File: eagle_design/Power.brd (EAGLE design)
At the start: 55.9 x 63.2 mm, 17 parts, among them K1 G5LE, K2 G5LE, K3 G5LE

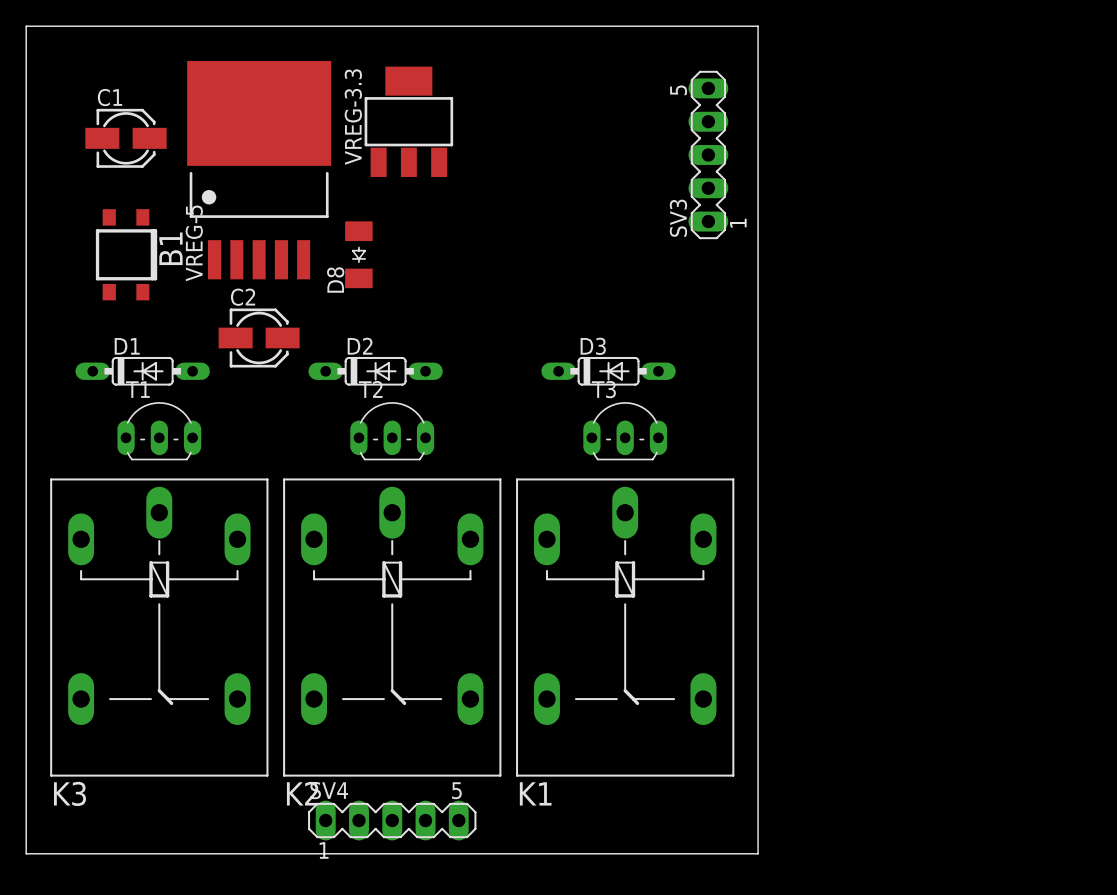
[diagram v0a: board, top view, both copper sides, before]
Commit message: split into three boards and choose new mcu
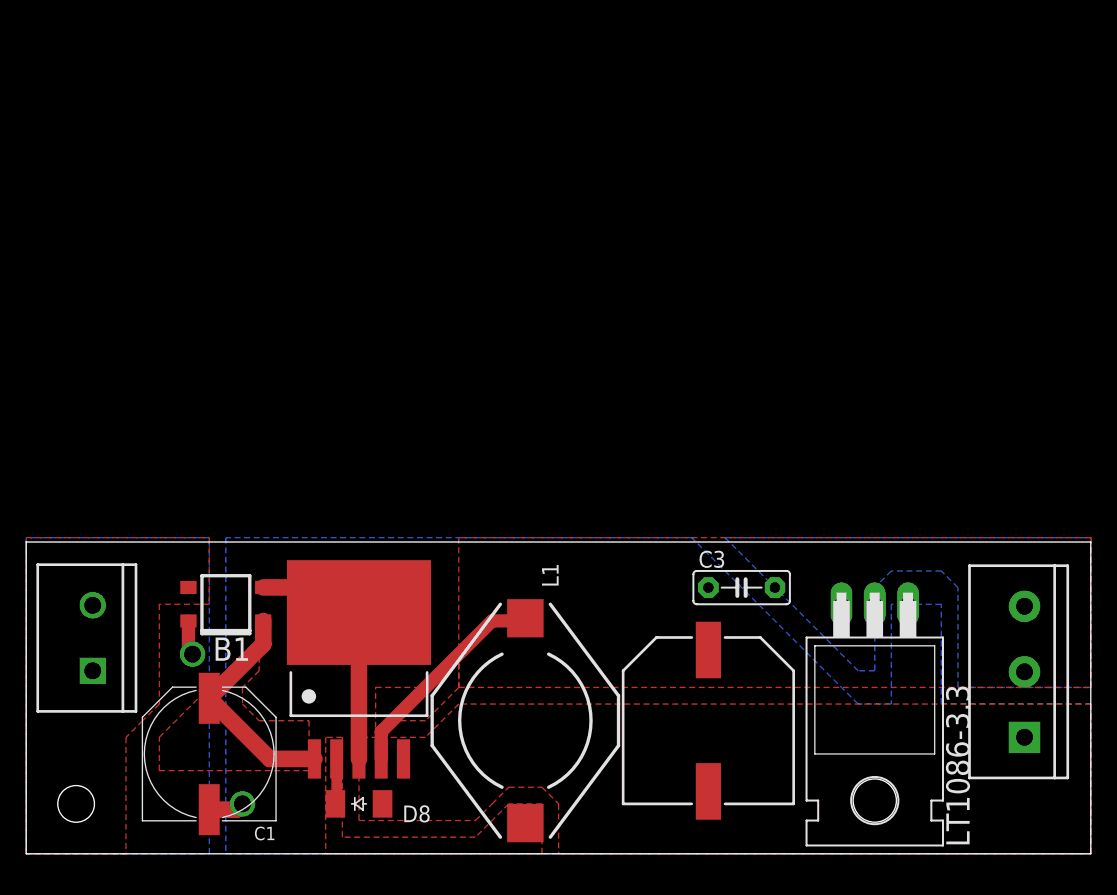
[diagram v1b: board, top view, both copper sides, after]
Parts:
- removed D1, D2, D3: 1N4148DO35-7, diode:DO35-7
- removed K1, K2, K3: G5LE, relay:G5LE
- removed SV3, SV4: (no value), con-lstb:MA05-1
- removed T1, T2, T3: (no value), transistor-neu-to92:TO92-EBC
- removed VREG-3.3: (no value), linear-technology:SOT223
- added C3: 10uF, capacitor-wima:C5B2.5
- added L1: 330uH, TylersLib:DO3316P
- added LT1086-3.3: 317T, linear:TO220H
- added U$1: SCREWTERMINAL-3, SparkFun-Connectors:SCREWTERMINAL-5MM-3
- added U$2: SCREWTERMINAL-2, SparkFun-Connectors:SCREWTERMINAL-5MM-2
- C1: device rcl:153CLV-0405 -> rcl:PANASONIC_G
- C2: value 330uF -> 300uF; device rcl:153CLV-0405 -> rc-master:CSV-H
- moved C1 47.4 mm to (14.0, 7.62), turned to 90 degrees
- moved C2 45.0 mm to (52.1, 10.2), turned to 270 degrees
- moved D8 41.9 mm to (25.4, 3.81), turned to 0 degrees
- moved VREG-5 38.9 mm to (20.3, 5.08)
- moved B1 27.7 mm to (15.2, 19.1), turned to 90 degrees
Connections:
- net N$1 renamed VUNREG
- removed net 3.3+: SV3.5, VREG-3.3.3
- removed net 5V+: C2.+, D1.C, D2.C, D3.C, K1.1, K2.1, K3.1, VREG-3.3.1, VREG-5.4
- removed net AC: SV3.2, T2.B
- removed net FAN: SV3.1, T1.B
- removed net G: K3.S, SV4.1
- removed net HEAT: SV3.3, T3.B
- removed net N$2: D1.A, K3.2, T1.C
- removed net N$3: D2.A, K2.2, T2.C
- removed net N$5: D3.A, K1.2, T3.C
- removed net N$6: K1.O
- removed net N$7: K2.O
- removed net N$8: K3.O
- removed net W: K1.S, SV4.3
- removed net Y: K2.S, SV4.2
- new net FIVE+: C2.+, L1.2, LT1086-3.3.3, U$1.3, VREG-5.4
- new net THREE+: C3.1, LT1086-3.3.2, U$1.2
- net GND: now also C3.2, LT1086-3.3.1, U$1.1; no longer SV3.4, T1.E, T2.E, T3.E, VREG-3.3.2, VREG-3.3.4
- net N$4: now also L1.1
- net VAC+: now also U$2.1; no longer K1.P, K2.P, K3.P, SV4.5
- net VAC-: now also B1.AC2, U$2.2; no longer SV4.4
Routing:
- net GND: track 0.00 -> 24.7 mm, vias 0 -> 1
- net VUNREG: track 0.00 -> 17.6 mm
- net FIVE+: track 0.00 -> 16.9 mm
- net N$4: track 0.00 -> 3.47 mm
- net VAC+: track 0.00 -> 2.66 mm, vias 0 -> 1
- added copper zone on layer 1, net FIVE+
- added copper zone on layer 1, net GND
- added copper zone on layer 16, net GND
- added copper zone on layer 1, net N$4
- added copper zone on layer 16, net THREE+
- added copper zone on layer 16, net VAC+
- added copper zone on layer 1, net VAC-
- added copper zone on layer 1, net VUNREG
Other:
- board size 55.9 x 63.2 mm -> 81.3 x 23.8 mm

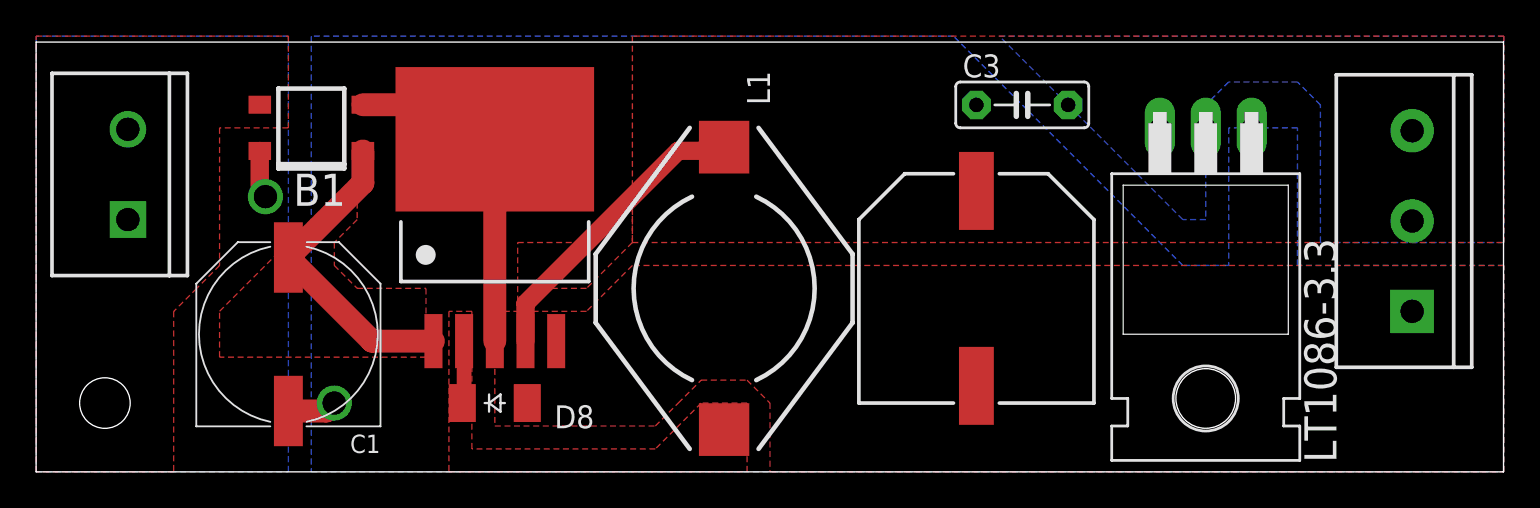
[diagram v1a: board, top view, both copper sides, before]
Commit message: made boards smaller
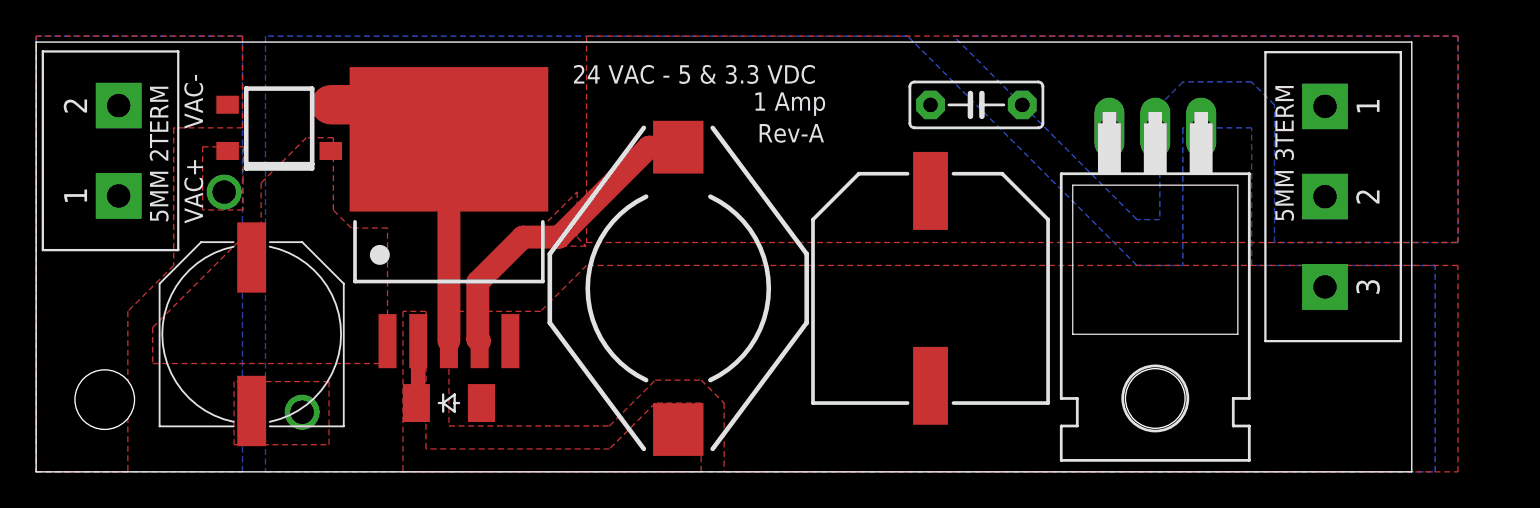
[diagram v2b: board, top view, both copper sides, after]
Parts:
- removed U$1: SCREWTERMINAL-3, SparkFun-Connectors:SCREWTERMINAL-5MM-3
- added U$3: OSTTC030162, TylersLib:OSTTC030162
- U$2: value SCREWTERMINAL-2 -> OSTTC020162; device SparkFun-Connectors:SCREWTERMINAL-5MM-2 -> TylersLib:OSTTC020162
- moved U$2 3.84 mm to (4.57, 17.8)
- moved LT1086-3.3 2.79 mm to (62.0, 8.89)
- moved C2 2.54 mm to (49.5, 10.2)
- moved C3 2.54 mm to (52.1, 20.3)
- moved D8 2.54 mm to (22.9, 3.81)
- moved L1 2.54 mm to (35.6, 8.89)
- moved VREG-5 2.54 mm to (17.8, 5.08)
- moved C1 2.03 mm to (11.9, 7.62)
- moved B1 1.78 mm to (13.5, 19.1)
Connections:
- net FIVE+: now also U$3.1; no longer U$1.3
- net GND: now also U$3.3; no longer U$1.1
- net THREE+: now also U$3.2; no longer U$1.2
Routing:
- net VUNREG: track 17.6 -> 0.00 mm
- net GND: track 24.7 -> 21.2 mm
- net VAC+: track 2.66 -> 0.00 mm
- net FIVE+: track 16.9 -> 17.5 mm
- added copper zone on layer 1, net VAC+
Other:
- board size 81.3 x 23.8 mm -> 76.2 x 23.8 mm
- board text added: "1 Amp"
- board text added: "24 VAC - 5 & 3.3 VDC"
- board text added: "Rev-A"
- board text added: "VAC+"
- board text added: "VAC-"

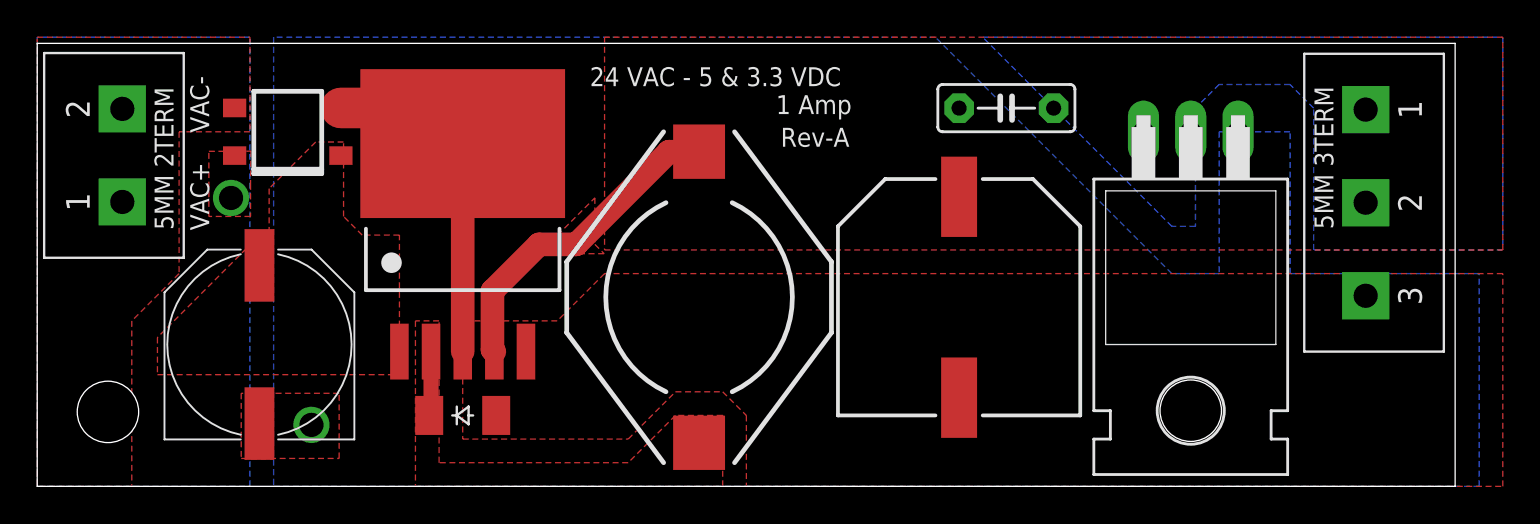
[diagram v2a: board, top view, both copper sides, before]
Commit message: Cleaned up boards and added script to gen gerbers
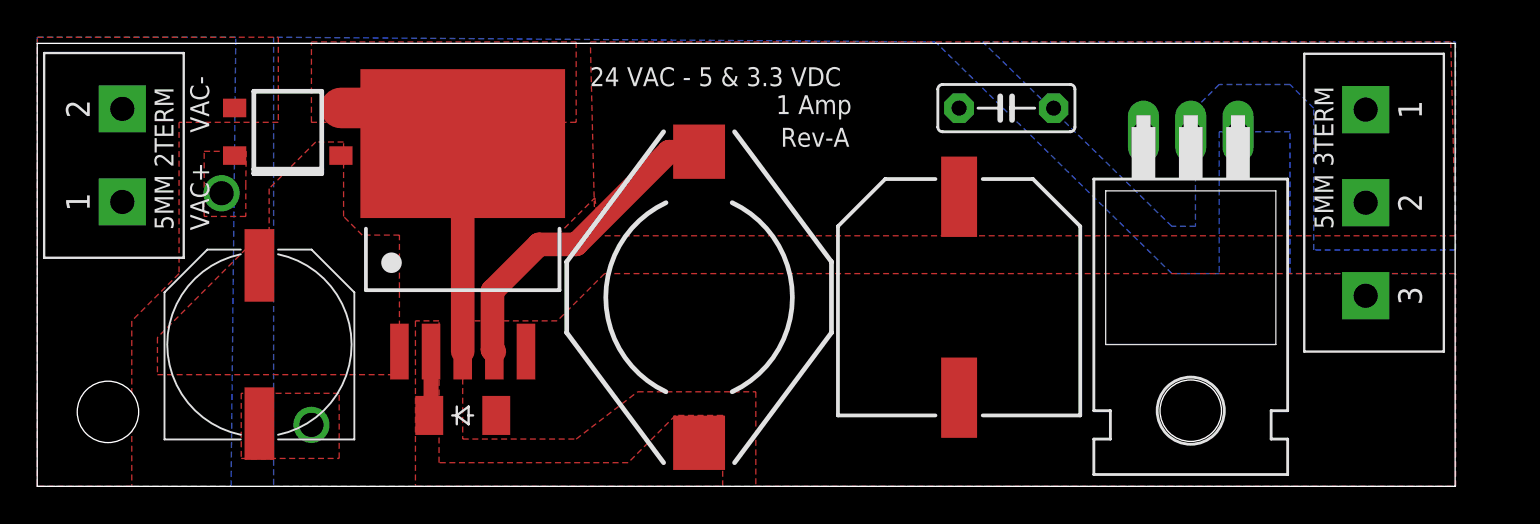
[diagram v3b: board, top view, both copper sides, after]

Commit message: more modifications
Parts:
- moved B1 0.76 mm to (12.7, 19.1)
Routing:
- net GND: track 21.2 -> 22.0 mm
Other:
- board text added: "3.3V"
- board text added: "5V"
- board text added: "GND"
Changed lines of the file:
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@@
 <drawing>
 <settings>
-<setting alwaysvectorfont="no"/>
+<setting alwaysvectorfont="yes"/>
 <setting verticaltext="up"/>
 </settings>
 <grid distance="0.01" unitdist="inch" unit="inch" style="lines" multiple="1" display="no" altdistance="0.025" altunitdist="inch" altunit="mm"/>
 <layers>
-<layer number="1" name="Top" color="4" fill="1" visible="yes" active="yes"/>
+<layer number="1" name="Top" color="4" fill="1" visible="no" active="yes"/>
 <layer number="2" name="Route2" color="1" fill="3" visible="no" active="no"/>
 <layer number="3" name="Route3" color="4" fill="3" visible="no" active="no"/>
@@
 <layer number="17" name="Pads" color="2" fill="1" visible="yes" active="yes"/>
 <layer number="18" name="Vias" color="2" fill="1" visible="yes" active="yes"/>
-<layer number="19" name="Unrouted" color="6" fill="1" visible="no" active="yes"/>
+<layer number="19" name="Unrouted" color="6" fill="1" visible="yes" active="yes"/>
 <layer number="20" name="Dimension" color="15" fill="1" visible="yes" active="yes"/>
 <layer number="21" name="tPlace" color="7" fill="1" visible="yes" active="yes"/>
-<layer number="22" name="bPlace" color="7" fill="1" visible="no" active="yes"/>
+<layer number="22" name="bPlace" color="7" fill="1" visible="yes" active="yes"/>
 <layer number="23" name="tOrigins" color="15" fill="1" visible="yes" active="yes"/>
-<layer number="24" name="bOrigins" color="15" fill="1" visible="no" active="yes"/>
+<layer number="24" name="bOrigins" color="15" fill="1" visible="yes" active="yes"/>
 <layer number="25" name="tNames" color="7" fill="1" visible="yes" active="yes"/>
-<layer number="26" name="bNames" color="7" fill="1" visible="no" active="yes"/>
+<layer number="26" name="bNames" color="7" fill="1" visible="yes" active="yes"/>
 <layer number="27" name="tValues" color="7" fill="1" visible="yes" active="yes"/>
-<layer number="28" name="bValues" color="7" fill="1" visible="no" active="yes"/>
+<layer number="28" name="bValues" color="7" fill="1" visible="yes" active="yes"/>
 <layer number="29" name="tStop" color="7" fill="3" visible="yes" active="yes"/>
 <layer number="30" name="bStop" color="7" fill="6" visible="yes" active="yes"/>
 <layer number="31" name="tCream" color="7" fill="4" visible="yes" active="yes"/>
-<layer number="32" name="bCream" color="7" fill="5" visible="no" active="yes"/>
-<layer number="33" name="tFinish" color="6" fill="3" visible="no" active="yes"/>
-<layer number="34" name="bFinish" color="6" fill="6" visible="no" active="yes"/>
+<layer number="32" name="bCream" color="7" fill="5" visible="yes" active="yes"/>
+<layer number="33" name="tFinish" color="6" fill="3" visible="yes" active="yes"/>
+<layer number="34" name="bFinish" color="6" fill="6" visible="yes" active="yes"/>
 <layer number="35" name="tGlue" color="7" fill="4" visible="no" active="yes"/>
 <layer number="36" name="bGlue" color="7" fill="5" visible="no" active="yes"/>
@@
 <layer number="40" name="bKeepout" color="1" fill="11" visible="no" active="yes"/>
 <layer number="41" name="tRestrict" color="4" fill="10" visible="no" active="yes"/>
-<layer number="42" name="bRestrict" color="1" fill="10" visible="yes" active="yes"/>
-<layer number="43" name="vRestrict" color="2" fill="10" visible="yes" active="yes"/>
+<layer number="42" name="bRestrict" color="1" fill="10" visible="no" active="yes"/>
+<layer number="43" name="vRestrict" color="2" fill="10" visible="no" active="yes"/>
 <layer number="44" name="Drills" color="7" fill="1" visible="yes" active="yes"/>
 <layer number="45" name="Holes" color="7" fill="1" visible="yes" active="yes"/>
@@
 <layer number="49" name="Reference" color="7" fill="1" visible="no" active="yes"/>
 <layer number="50" name="dxf" color="7" fill="1" visible="no" active="yes"/>
-<layer number="51" name="tDocu" color="7" fill="1" visible="yes" active="yes"/>
+<layer number="51" name="tDocu" color="7" fill="1" visible="no" active="yes"/>
 <layer number="52" name="bDocu" color="7" fill="1" visible="no" active="yes"/>
 <layer number="53" name="tGND_GNDA" color="7" fill="9" visible="no" active="no"/>
@@
 <wire x1="76.18" y1="23.8" x2="0" y2="23.8" width="0" layer="20"/>
 <wire x1="0" y1="23.8" x2="0" y2="0" width="0" layer="20"/>
-<text x="39.944" y="18.246" size="1.016" layer="21">Rev-A</text>
-<text x="29.69" y="21.5" size="1.016" layer="21">24 VAC - 5 &amp; 3.3 VDC</text>
-<text x="9.238" y="19" size="1.016" layer="21" rot="R90">VAC-</text>
-<text x="9.238" y="13.754" size="1.016" layer="21" rot="R90">VAC+</text>
-<text x="39.69" y="20" size="1.016" layer="21">1 Amp</text>
+<text x="42.992" y="18.246" size="1.016" layer="21">Rev-A</text>
+<text x="29.436" y="21.5" size="1.016" layer="21">24 VAC - 5 &amp; 3.3 VDC</text>
+<text x="42.992" y="20" size="1.016" layer="21">1 Amp</text>
 <hole x="3.8" y="4" drill="3.3"/>
+<text x="7.874" y="17.272" size="1.016" layer="26" rot="MR270">VAC+</text>
+<text x="8.128" y="21.844" size="1.016" layer="26" rot="MR270">VAC-</text>
+<text x="74.676" y="21.082" size="1.016" layer="26" rot="MR270">5V</text>
+<text x="74.93" y="16.764" size="1.016" layer="26" rot="MR270">3.3V</text>
+<text x="74.93" y="11.684" size="1.016" layer="26" rot="MR270">GND</text>
 </plain>
 <attributes>
@@
 <element name="VREG-5" library="texas" package="TO-263-5" value="TL2575-05" x="17.78" y="5.08" smashed="yes"/>
 <element name="D8" library="diode" package="SOD-123_MINI-SMA" value="CGRM4001-G" x="22.86" y="3.81" smashed="yes"/>
-<element name="B1" library="rectifier" package="TO-269AA" value="RECTIFIER-S80" x="13.462" y="19.05" smashed="yes" rot="R90"/>
+<element name="B1" library="rectifier" package="TO-269AA" value="RECTIFIER-S80" x="12.7" y="19.05" smashed="yes" rot="R90"/>
 <element name="C1" library="rcl" package="PANASONIC_G" value="100uF" x="11.938" y="7.62" smashed="yes" rot="R90"/>
 <element name="C2" library="rc-master" package="CSV-H" value="300uF" x="49.53" y="10.16" smashed="yes" rot="R270"/>
@@
 <contactref element="C3" pad="2"/>
 <wire x1="24.765" y1="20.32" x2="22.86" y2="18.415" width="1.27" layer="1"/>
-<via x="14.732" y="3.302" extent="1-16" drill="1.3"/>
+<via x="14.732" y="1.524" extent="1-16" drill="1.3"/>
 <polygon width="0.254" layer="1" isolate="0.3048">
 <vertex x="76.2" y="11.43"/>
@@
 </polygon>
 <contactref element="U$3" pad="3"/>
-<wire x1="16.317" y1="20.33" x2="20.945" y2="20.33" width="2.1844" layer="1"/>
+<wire x1="15.555" y1="20.33" x2="20.945" y2="20.33" width="2.1844" layer="1"/>
 <wire x1="20.945" y1="20.33" x2="22.86" y2="18.415" width="2.1844" layer="1"/>
 <polygon width="0.254" layer="1" isolate="0.3048">
-<vertex x="10.96" y="1.5"/>
-<vertex x="16.222" y="1.5"/>
+<vertex x="10.96" y="-0.024"/>
+<vertex x="16.222" y="-0.024"/>
 <vertex x="16.222" y="5"/>
 <vertex x="10.96" y="5"/>
@@
 <signal name="VAC+">
 <contactref element="B1" pad="AC1"/>
-<via x="9.906" y="15.748" extent="1-16" drill="1.3"/>
+<via x="9.906" y="15.494" extent="1-16" drill="1.3"/>
 <polygon width="0.254" layer="16" isolate="0.3048">
 <vertex x="10.414" y="0"/>
@@
 <vertex x="11.23" y="18.008"/>
 <vertex x="11.206" y="16.254"/>
-<vertex x="11.206" y="14.5"/>
-<vertex x="8.968" y="14.5"/>
+<vertex x="11.206" y="14.246"/>
+<vertex x="8.968" y="14.246"/>
 <vertex x="8.968" y="18"/>
 <vertex x="10.722" y="18"/>
